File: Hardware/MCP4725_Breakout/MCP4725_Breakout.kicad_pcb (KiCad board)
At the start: 2 copper layers, 15.2 x 15.2 mm, 17 parts, among them U1 MCP4725

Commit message: Saves progress
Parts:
- removed FRAME2: , MCP4725_Breakout:CREATIVE_COMMONS
- removed GND0: LOGO-SFESK, MCP4725_Breakout:SFE-LOGO-FLAME
- removed JP5: , MCP4725_Breakout:1X04
- removed JP6: M02PTH, MCP4725_Breakout:1X02
- removed LOGO1: OSHW-LOGOS, MCP4725_Breakout:OSHW-LOGO-S
- removed R2: 4.7k, MCP4725_Breakout:0603-RES
- removed R3: 10k, MCP4725_Breakout:0603-RES
- removed SJ1: , MCP4725_Breakout:PAD-JUMPER-3-3OF3_NC_BY_TRACE_YES_SILK_FULL_BOX
- removed SJ2: JUMPER-PAD-3-2OF3_NC_BY_PASTE, MCP4725_Breakout:PAD-JUMPER-3-2OF3_NC_BY_PASTE_YES_SILK_FULL_BOX
- removed STANDOFF1, STANDOFF2: STAND-OFF, MCP4725_Breakout:STAND-OFF
- removed U$3: , MCP4725_Breakout:SFE_LOGO_FLAME_.2
- removed U1: MCP4725, MCP4725_Breakout:SOT23-6
- added FID3: Fiducial_0.5mm, SparkFun-Aesthetic:Fiducial_0.5mm_Mask1mm, F.Cu at (145.4, 111.8)
- added FID4: Fiducial_0.5mm, SparkFun-Aesthetic:Fiducial_0.5mm_Mask1mm, B.Cu at (145.4, 111.8)
- added G***: Flame, SparkFun-Aesthetic:SparkFun_Flame_3mm, F.Cu at (151.8, 101.6)
- added G1: OSHW_Logo, SparkFun-Aesthetic:Creative_Commons_License, F.Cu at (175.3, 110.4)
- added J1: Conn_01x02, SparkFun-Connector:1x02_P2.54mm, F.Cu at (142.2, 98.7)
- added J2: I2C, SparkFun-Connector:1x04_P2.54mm, F.Cu at (142.2, 111.4)
- added JP1: I2C, SparkFun-Jumper:Jumper_3_NC-2_Trace, B.Cu at (148.9, 110.9)
- added JP2: ADDR, SparkFun-Jumper:Jumper_3_NC-1_Trace, B.Cu at (148.9, 99.4)
- added R4: 4.7k, SparkFun-Resistor:R_0603_1608Metric, F.Cu at (150.8, 108.3)
- added R5: 4.7k, SparkFun-Resistor:R_0603_1608Metric, F.Cu at (149.2, 108.3)
- added Ref**: Val**, SparkFun-Aesthetic:OSHW_Logo_4mm, B.Cu at (149.5, 105.4)
- added ST1: Standoff, SparkFun-Hardware:Standoff, F.Cu at (154.3, 99.4)
- added ST2: Standoff, SparkFun-Hardware:Standoff, F.Cu at (154.3, 110.8)
- added U2: MCP4725, SparkFun-Semiconductor-Standard:SOT23-6, F.Cu at (150.8, 104.8)
- added kibuzzard-69B46D81: G***, kibuzzard-69B46D81, F.Cu at (144.8, 98.7)
- added kibuzzard-69B46D81: G***, kibuzzard-69B46D81, B.Cu at (144.8, 98.7)
- added kibuzzard-69B46D94: G***, kibuzzard-69B46D94, F.Cu at (144.5, 111.4)
- added kibuzzard-69B46D94: G***, kibuzzard-69B46D94, F.Cu at (144.5, 101.3)
- added kibuzzard-69B46D94: G***, kibuzzard-69B46D94, B.Cu at (144.5, 101.3)
- added kibuzzard-69B46D94: G***, kibuzzard-69B46D94, B.Cu at (144.5, 111.4)
- added kibuzzard-69B46DE0: G***, kibuzzard-69B46DE0, F.Cu at (144.5, 108.9)
- added kibuzzard-69B46DE0: G***, kibuzzard-69B46DE0, B.Cu at (144.5, 108.9)
- added kibuzzard-69B46E1A: G***, kibuzzard-69B46E1A, F.Cu at (154.6, 105.1)
- added kibuzzard-69B46E1A: G***, kibuzzard-69B46E1A, B.Cu at (153.0, 105.1)
- added kibuzzard-69B46E2A: G***, kibuzzard-69B46E2A, F.Cu at (144.8, 103.8)
- added kibuzzard-69B46E2F: G***, kibuzzard-69B46E2F, F.Cu at (144.8, 106.4)
- added kibuzzard-69B46E79: G***, kibuzzard-69B46E79, B.Cu at (148.9, 101.3)
- added kibuzzard-69B46E88: G***, kibuzzard-69B46E88, B.Cu at (148.9, 108.9)
- added kibuzzard-69B46EE5: G***, kibuzzard-69B46EE5, B.Cu at (144.8, 106.4)
- added kibuzzard-69B46EEC: G***, kibuzzard-69B46EEC, B.Cu at (144.8, 103.8)
- C1: footprint MCP4725_Breakout:0603-CAP -> SparkFun-Capacitor:C_0603_1608Metric
- FID1: value FIDUCIAL1X2 -> Fiducial_0.5mm; footprint MCP4725_Breakout:FIDUCIAL-1X2 -> SparkFun-Aesthetic:Fiducial_0.5mm_Mask1mm; moved to B.Cu
- FID2: value FIDUCIAL1X2 -> Fiducial_0.5mm; footprint MCP4725_Breakout:FIDUCIAL-1X2 -> SparkFun-Aesthetic:Fiducial_0.5mm_Mask1mm
- R1: value 4.7k -> 10k; footprint MCP4725_Breakout:0603-RES -> SparkFun-Resistor:R_0603_1608Metric
- moved FID1 13.5 mm to (152.4, 98.1), turned to 180 degrees
- moved C1 5.04 mm to (147.6, 104.8)
- moved FID2 3.64 mm to (152.4, 98.1)
- moved R1 0.73 mm to (149.2, 100.6), turned to 90 degrees
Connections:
- C1 pad 1: VCC -> 3.3V
- R1 pad 1: SCL -> GND
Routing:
- net VCC: track 32.8 -> 0.00 mm, vias 1 -> 0
- net 3.3V: track 0.00 -> 21.1 mm, vias 0 -> 1
- net N$3: track 7.61 -> 0.00 mm
- net ADDR: track 0.00 -> 7.08 mm, vias 0 -> 1
- net SDA: track 8.89 -> 15.3 mm
- net Net-(JP2-C): track 6.09 -> 0.91 mm
- net VOUT: track 14.7 -> 9.56 mm, vias 1 -> 0
- net SCL: track 17.1 -> 12.1 mm, vias 2 -> 0
- net N$1: track 3.98 -> 0.00 mm, vias 1 -> 0
- net Net-(JP1-A): track 0.00 -> 2.92 mm, vias 0 -> 1
- net Net-(JP1-C): track 0.00 -> 2.43 mm, vias 0 -> 1
- net GND: track 0.00 -> 2.20 mm, vias 2 -> 16
- net N$4: track 2.18 -> 0.00 mm
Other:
- rule pad_to_mask_clearance: 0 -> 0.127
- board text added: "V20"
- board text removed: "ADDR"
- board text removed: "GND"
- board text removed: "I2C"
- board text removed: "Joel Bartlett"
- board text removed: "MCP4725"
- board text removed: "OUT"
- board text removed: "PULLUPS"
- board text removed: "SCL"
- board text removed: "SDA"
- board text removed: "V14"
- board text removed: "VCC"

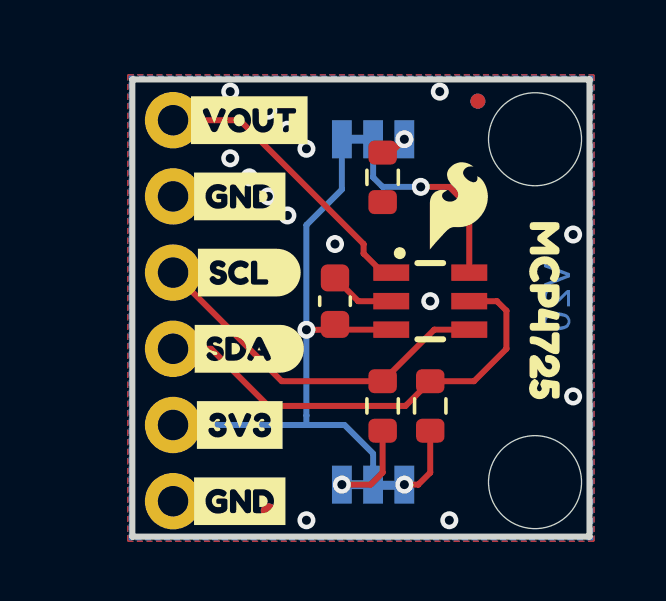
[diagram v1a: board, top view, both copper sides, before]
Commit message: Adjusts the jumpers on the underside
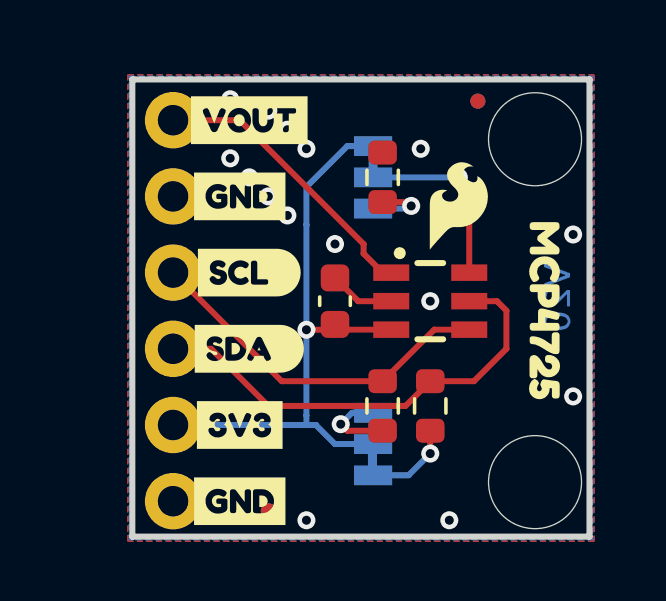
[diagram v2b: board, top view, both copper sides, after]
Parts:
- removed the Ref** at (149.5, 105.4)
- removed kibuzzard-69B46E79: G***, kibuzzard-69B46E79
- added G***: Flame, SparkFun-Aesthetic:SparkFun_Flame_2mm, B.Cu at (154.7, 101.9)
- added Ref**: Val**, SparkFun-Aesthetic:OSHW_Logo_2.5mm, B.Cu at (148.1, 104.9)
- added kibuzzard-69B976CB: G***, kibuzzard-69B976CB, B.Cu at (150.6, 100.6)
- added kibuzzard-69B9770D: G***, kibuzzard-69B9770D, B.Cu at (148.9, 98.4)
- added kibuzzard-69B97714: G***, kibuzzard-69B97714, B.Cu at (148.9, 102.9)
- moved kibuzzard-69B46E88 2.01 mm to (150.8, 109.5), turned to 90 degrees
- moved JP1 1.35 mm to (148.9, 109.5), turned to -90 degrees
- moved JP2 1.27 mm to (148.9, 100.6), turned to -90 degrees
- turned R1 to -90 degrees
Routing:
- net Net-(JP2-C): track 0.91 -> 2.31 mm
- net ADDR: track 7.08 -> 6.18 mm
- net Net-(JP1-C): track 2.43 -> 2.97 mm

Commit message: Saves progress before shifting board placement around screw terminals
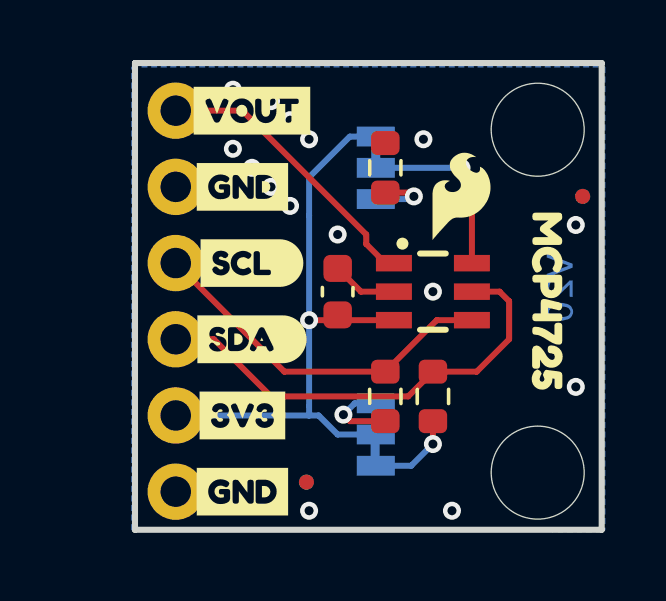
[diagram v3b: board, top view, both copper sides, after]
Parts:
- moved G1 67.2 mm to (226.3, 154.1)
- moved FID1 4.72 mm to (155.9, 101.3)
- moved FID2 4.72 mm to (155.9, 101.3)
- moved FID3 1.59 mm to (146.7, 110.8)
- moved FID4 1.59 mm to (146.7, 110.8)
- moved C1 0.33 mm to (147.7, 104.5)
- moved J1 0.33 mm to (142.3, 98.4)
- moved ST2 0.33 mm to (154.4, 110.5)
- moved U2 0.33 mm to (150.9, 104.5)
- moved kibuzzard-69B46D81 0.33 mm to (144.9, 98.4) (x2)
- moved kibuzzard-69B46DE0 0.33 mm to (144.6, 108.6) (x2)
- moved kibuzzard-69B46E2A 0.33 mm to (144.9, 103.5)
- moved kibuzzard-69B46EEC 0.33 mm to (144.9, 103.5)
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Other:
- board size 15.2 x 15.2 mm -> 15.6 x 15.6 mm

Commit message: Moves the entire board such that the stand offs and plated through holes
...are evenly spaced relative to the edge. The standoffs and plated
through holes did not move relative to each other.
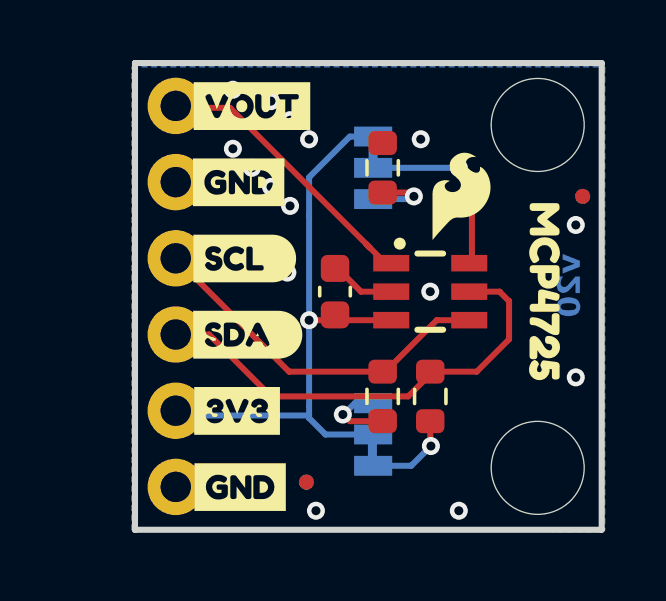
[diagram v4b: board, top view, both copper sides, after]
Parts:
- moved kibuzzard-69B46E1A 0.33 mm to (154.6, 104.5)
- moved kibuzzard-69B46E1A 0.32 mm to (153.1, 104.5)
- moved kibuzzard-69B46E2A 0.29 mm to (144.6, 103.4)
- moved kibuzzard-69B46EEC 0.29 mm to (144.6, 103.4)
- moved kibuzzard-69B46DE0 0.23 mm to (144.4, 108.4) (x2)
- moved kibuzzard-69B46E2F 0.21 mm to (144.7, 105.9)
- moved kibuzzard-69B46EE5 0.21 mm to (144.7, 105.9)
- moved kibuzzard-69B46D94 0.20 mm to (144.4, 100.8) (x2)
- moved kibuzzard-69B46D94 0.17 mm to (144.5, 111.0) (x2)
- moved J1 0.16 mm to (142.3, 98.3)
- moved J2 0.16 mm to (142.3, 111.0)
- moved ST1 0.16 mm to (154.4, 98.9)
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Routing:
- net GND: vias 16 -> 15
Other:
- board text added: "v20"
- board text removed: "V20"

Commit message: Fixes DAC symbol, aligns Qwiic connector, removes extra pour
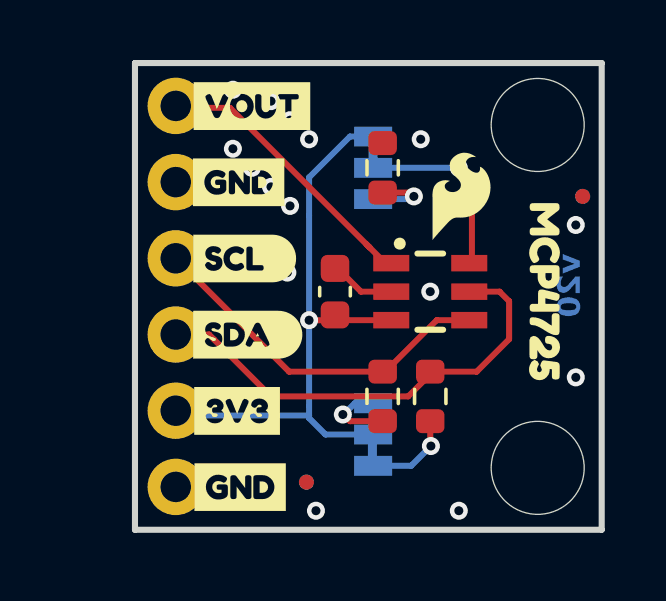
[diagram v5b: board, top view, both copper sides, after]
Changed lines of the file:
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@@
 				(font
 					(size 0.001 0.001)
+					(thickness 0.15)
 				)
 				(justify mirror)
@@
 				(font
 					(size 0.001 0.001)
+					(thickness 0.15)
 				)
 				(justify mirror)
@@
 				(font
 					(size 0.001 0.001)
+					(thickness 0.15)
 				)
 				(justify mirror)
@@
 				(font
 					(size 0.001 0.001)
+					(thickness 0.15)
 				)
 				(justify mirror)
@@
 				(font
 					(size 0.001 0.001)
+					(thickness 0.15)
 				)
 				(justify mirror)
@@
 				(font
 					(size 0.001 0.001)
+					(thickness 0.15)
 				)
 				(justify mirror)
@@
 			)
 		)
-	)
-	(zone
-		(net 1)
-		(net_name "GND")
-		(layer "B.Cu")
-		(hatch edge 0.5)
-		(priority 6)
-		(connect_pads
-			(clearance 0.3048)
-		)
-		(min_thickness 0.1016)
-		(filled_areas_thickness no)
-		(fill yes
-			(thermal_gap 0.2532)
-			(thermal_bridge_width 0.2532)
-		)
-		(polygon
-			(pts
-				(xy 156.6291 112.4077) (xy 140.8684 112.4077) (xy 140.8684 96.9645) (xy 156.6291 96.9645)
-			)
-		)

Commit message: Fixes swapped pins on SCL/SDA
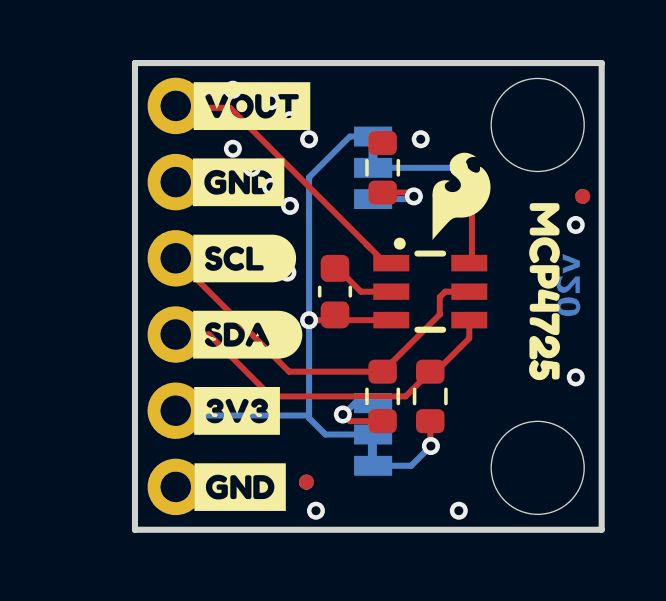
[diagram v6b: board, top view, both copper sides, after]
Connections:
- U2 pad 4: SCL -> SDA
- U2 pad 5: SDA -> SCL
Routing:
- net SDA: track 15.4 -> 12.0 mm
- net SCL: track 12.1 -> 12.8 mm
- net GND: vias 15 -> 14
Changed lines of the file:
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@@
 			(size 0.55 1.2)
 			(layers "F.Cu" "F.Mask" "F.Paste")
-			(net 3 "SCL")
+			(net 4 "SDA")
 			(pinfunction "SDA")
 			(pintype "bidirectional")
@@
 			(size 0.55 1.2)
 			(layers "F.Cu" "F.Mask" "F.Paste")
-			(net 4 "SDA")
+			(net 3 "SCL")
 			(pinfunction "SCL")
 			(pintype "bidirectional")
@@
 	)
 	(via
-		(at 150.8125 104.4575)
-		(size 0.6)
-		(drill 0.3)
-		(layers "F.Cu" "B.Cu")
-		(free yes)
-		(net 1)
-	)
-	(via
 		(at 155.6639 102.235)
 		(size 0.6)
@@
 	)
 	(segment
-		(start 152.2015 105.4075)
-		(end 151.0314 105.4075)
+		(start 151.13 104.64)
+		(end 151.13 105.22)
 		(width 0.2)
 		(layer "F.Cu")
@@
 	)
 	(segment
-		(start 146.10765 107.125)
-		(end 149.225 107.125)
+		(start 151.3125 104.4575)
+		(end 151.13 104.64)
 		(width 0.2)
 		(layer "F.Cu")
@@
 	)
 	(segment
-		(start 151.0314 105.4075)
-		(end 149.3139 107.125)
+		(start 149.225 107.125)
+		(end 146.10765 107.125)
 		(width 0.2)
 		(layer "F.Cu")
@@
 	)
 	(segment
-		(start 143.44015 105.88625)
-		(end 143.5989 106.045)
+		(start 152.1125 104.4575)
+		(end 151.3125 104.4575)
 		(width 0.2)
 		(layer "F.Cu")
-		(net 4)
-	)
-	(segment
-		(start 142.3289 105.88625)
-		(end 143.44015 105.88625)
-		(width 0.2)
-		(layer "F.Cu")
-		(net 4)
+		(net 3)
 	)
 	(segment
-		(start 152.2014 104.4575)
-		(end 153.1239 104.4575)
+		(start 151.13 105.22)
+		(end 149.225 107.125)
 		(width 0.2)
 		(layer "F.Cu")
-		(net 4)
+		(net 3)
 	)
 	(segment
-		(start 150.9014 107.125)
-		(end 150.0764 107.95)
+		(start 152.1126 106.0149)
+		(end 151.0025 107.125)
 		(width 0.2)
 		(layer "F.Cu")
@@
 	)
 	(segment
-		(start 153.4414 106.045)
-		(end 152.3614 107.125)
+		(start 151.0025 107.125)
+		(end 150.8125 107.125)
 		(width 0.2)
 		(layer "F.Cu")
@@
 	)
 	(segment
-		(start 152.3614 107.125)
-		(end 150.9014 107.125)
+		(start 149.9875 107.95)
+		(end 145.5039 107.95)
 		(width 0.2)
 		(layer "F.Cu")
@@
 	)
 	(segment
-		(start 150.0764 107.95)
-		(end 145.5039 107.95)
+		(start 150.8125 107.125)
+		(end 149.9875 107.95)
 		(width 0.2)
 		(layer "F.Cu")
@@
 	)
 	(segment
-		(start 153.1239 104.4575)
-		(end 153.4414 104.775)
+		(start 152.1126 105.4075)
+		(end 152.1126 106.0149)
 		(width 0.2)
 		(layer "F.Cu")
@@
 	)
 	(segment
-		(start 153.4414 104.775)
-		(end 153.4414 106.045)
+		(start 143.44015 105.88625)
+		(end 142.3289 105.88625)
 		(width 0.2)
 		(layer "F.Cu")
@@
 	(segment
 		(start 145.5039 107.95)
-		(end 143.5989 106.045)
+		(end 143.44015 105.88625)
 		(width 0.2)
 		(layer "F.Cu")

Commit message: Adds new gitignore
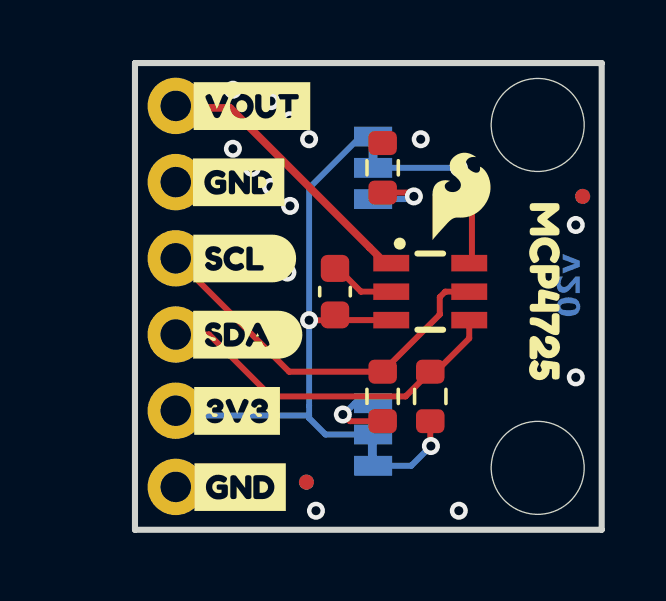
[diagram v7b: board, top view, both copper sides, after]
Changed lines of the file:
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@@
 	)
 	(segment
-		(start 146.7739 100.6475)
-		(end 146.7739 101.9175)
-		(width 0.2)
-		(layer "B.Cu")
-		(net 2)
-	)
-	(segment
-		(start 148.9964 99.2886)
-		(end 148.1328 99.2886)
+		(start 146.7739 101.0031)
+		(end 146.7739 105.41)
 		(width 0.2)
 		(layer "B.Cu")
@@
 	)
 	(segment
+		(start 148.9964 99.2886)
+		(end 148.4884 99.2886)
+		(width 0.2)
+		(layer "B.Cu")
+		(net 2)
+	)
+	(segment
 		(start 147.32 109.22)
 		(end 146.7739 108.6739)
@@
 	)
 	(segment
-		(start 146.7739 105.41)
-		(end 146.7739 101.9175)
-		(width 0.2)
-		(layer "B.Cu")
-		(net 2)
-	)
-	(segment
 		(start 146.7739 108.2675)
 		(end 146.7739 105.41)
@@
 	)
 	(segment
+		(start 148.4884 99.2886)
+		(end 146.7739 101.0031)
+		(width 0.2)
+		(layer "B.Cu")
+		(net 2)
+	)
+	(segment
 		(start 146.7739 108.6739)
 		(end 146.7739 108.585)
@@
 		(start 142.3289 108.585)
 		(end 146.7739 108.585)
-		(width 0.2)
-		(layer "B.Cu")
-		(net 2)
-	)
-	(segment
-		(start 148.1328 99.2886)
-		(end 146.7739 100.6475)
 		(width 0.2)
 		(layer "B.Cu")
@@
 		(start 144.1396 98.3307)
 		(end 148.7932 102.9843)
-		(width 0.2)
+		(width 0.254)
 		(layer "F.Cu")
 		(net 8)
@@
 		(start 142.39335 98.3307)
 		(end 144.1396 98.3307)
-		(width 0.2)
+		(width 0.254)
 		(layer "F.Cu")
 		(net 8)
@@
 		(start 149.3164 103.5075)
 		(end 148.7932 102.9843)
-		(width 0.2)
+		(width 0.254)
 		(layer "F.Cu")
 		(net 8)
